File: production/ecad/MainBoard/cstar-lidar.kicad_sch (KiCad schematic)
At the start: 0 parts

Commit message: Added Lidar Connector
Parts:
- added J1: 532610771, 532610771:MOLEX_532610771, symbol 532610771:532610771
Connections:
- new net GND: J1.3, J1.4
- new net P3V3: J1.2
- new net P5V: J1.1, J1.5
- new net RX: J1.7
- new net TX: J1.6
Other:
- note added: "Lidar Connector"
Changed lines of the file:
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@@
 (kicad_sch (version 20230121) (generator eeschema)
   (paper "A4")
+  (wire (pts (xy 134.62 60.96) (xy 124.46 60.96))
+    (stroke (width 0) (type default))
+  )
+  (wire (pts (xy 124.46 66.04) (xy 134.62 66.04))
+    (stroke (width 0) (type default))
+  )
+  (wire (pts (xy 124.46 63.5) (xy 134.62 63.5))
+    (stroke (width 0) (type default))
+  )
+  (wire (pts (xy 124.46 73.66) (xy 134.62 73.66))
+    (stroke (width 0) (type default))
+  )
+  (wire (pts (xy 124.46 68.58) (xy 134.62 68.58))
+    (stroke (width 0) (type default))
+  )
+  (wire (pts (xy 124.46 71.12) (xy 134.62 71.12))
+    (stroke (width 0) (type default))
+  )
+  (wire (pts (xy 124.46 76.2) (xy 134.62 76.2))
+    (stroke (width 0) (type default))
+  )
+  (text "Lidar Connector\n" (at 134.62 53.34 0)
+    (effects (font (size 2 2)) (justify left bottom))
+  )
+  (label "GND" (at 124.46 68.58 0) (fields_autoplaced)
+    (effects (font (size 1.27 1.27)) (justify left bottom))
+  )
+  (label "TX" (at 124.46 73.66 0) (fields_autoplaced)
+    (effects (font (size 1.27 1.27)) (justify left bottom))
+  )
+  (label "GND" (at 124.46 66.04 0) (fields_autoplaced)
+    (effects (font (size 1.27 1.27)) (justify left bottom))
+  )
+  (label "RX" (at 124.46 76.2 0) (fields_autoplaced)
+    (effects (font (size 1.27 1.27)) (justify left bottom))
+  )
+  (label "P5V" (at 124.46 60.96 0) (fields_autoplaced)
+    (effects (font (size 1.27 1.27)) (justify left bottom))
+  )
+  (label "P5V" (at 124.46 71.12 0) (fields_autoplaced)
+    (effects (font (size 1.27 1.27)) (justify left bottom))
+  )
+  (label "P3V3" (at 124.46 63.5 0) (fields_autoplaced)
+    (effects (font (size 1.27 1.27)) (justify left bottom))
+  )
+  (symbol (lib_id "532610771:532610771") (at 147.32 71.12 0) (unit 1)
+    (in_bom yes) (on_board yes) (dnp no) (fields_autoplaced)
+    (property "Reference" "J1" (at 156.21 71.12 0)
+      (effects (font (size 1.27 1.27)) (justify left))
+    )
+    (property "Value" "532610771" (at 156.21 73.66 0)
+      (effects (font (size 1.27 1.27)) (justify left))
+    )
+    (property "Footprint" "532610771:MOLEX_532610771" (at 147.32 71.12 0)
+      (effects (font (size 1.27 1.27)) (justify bottom) hide)
+    )
+    (property "Datasheet" "" (at 147.32 71.12 0)
+      (effects (font (size 1.27 1.27)) hide)
+    )
+    (property "DigiKey_Part_Number" "WM7625TR-ND" (at 147.32 71.12 0)
+      (effects (font (size 1.27 1.27)) (justify bottom) hide)
+    )
+    (property "MF" "Molex" (at 147.32 71.12 0)
+      (effects (font (size 1.27 1.27)) (justify bottom) hide)
+    )
+    (property "MAXIMUM_PACKAGE_HEIGHT" "3.4 mm" (at 147.32 71.12 0)
+      (effects (font (size 1.27 1.27)) (justify bottom) hide)
+    )
+    (property "Package" "None" (at 147.32 71.12 0)
+      (effects (font (size 1.27 1.27)) (justify bottom) hide)
+    )
+    (property "Check_prices" "https://www.snapeda.com/parts/0532610771/Molex/view-part/?ref=eda" (at 147.32 71.12 0)
+      (effects (font (size 1.27 1.27)) (justify bottom) hide)
+    )
+    (property "STANDARD" "Manufacturer Recommendations" (at 147.32 71.12 0)
+      (effects (font (size 1.27 1.27)) (justify bottom) hide)
+    )
+    (property "PARTREV" "J" (at 147.32 71.12 0)
+      (effects (font (size 1.27 1.27)) (justify bottom) hide)
+    )
+    (property "SnapEDA_Link" "https://www.snapeda.com/parts/0532610771/Molex/view-part/?ref=snap" (at 147.32 71.12 0)
+      (effects (font (size 1.27 1.27)) (justify bottom) hide)
+    )
+    (property "MP" "0532610771" (at 147.32 71.12 0)
+      (effects (font (size 1.27 1.27)) (justify bottom) hide)
+    )
+    (property "Purchase-URL" "https://www.snapeda.com/api/url_track_click_mouser/?unipart_id=577144&manufacturer=Molex&part_name=0532610771&search_term=None" (at 147.32 71.12 0)
+      (effects (font (size 1.27 1.27)) (justify bottom) hide)
+    )
+    (property "Description" "\nPicoblade Connector, 7 Circuit Single Row, Right Angle Surface Mount SMT PCB\n" (at 147.32 71.12 0)
+      (effects (font (size 1.27 1.27)) (justify bottom) hide)
+    )
+    (property "MANUFACTURER" "Molex" (at 147.32 71.12 0)
+      (effects (font (size 1.27 1.27)) (justify bottom) hide)
+    )
+    (pin "S2")
+    (pin "2")
+    (pin "3")
+    (pin "S1")
+    (pin "5")
+    (pin "4")
+    (pin "6")
+    (pin "7")
+    (pin "1")
+    (instances
+      (project "cstar-lidar"
+        (path "/f4254b98-3297-4812-862b-6470cd23e6be"
+          (reference "J1") (unit 1)
+        )
+      )
+    )
+  )
+  (sheet_instances
+    (path "/" (page "1"))
+  )
 )

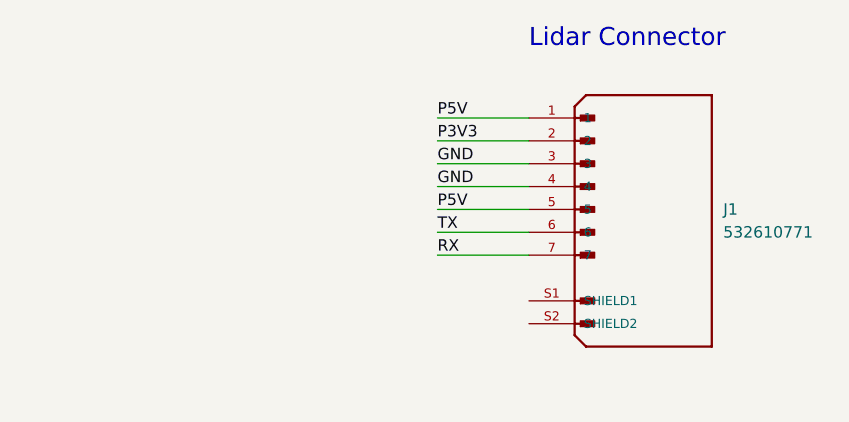
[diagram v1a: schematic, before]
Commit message: Added global and hierarchical connection for the lidar connector
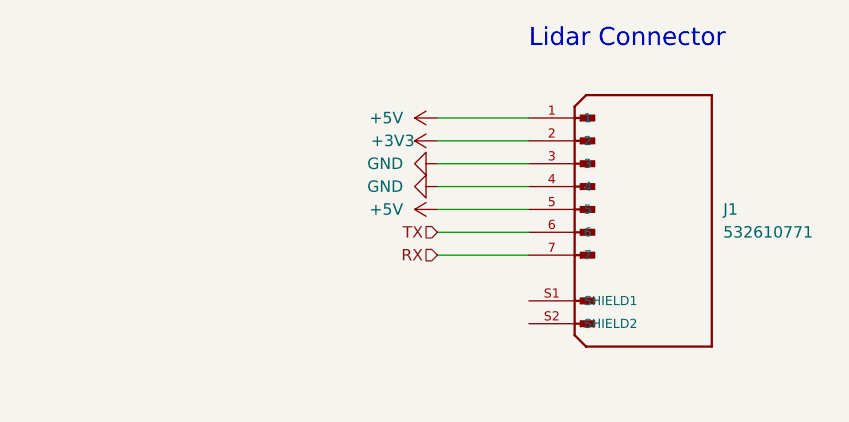
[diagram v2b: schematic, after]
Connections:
- net P3V3 renamed +3V3
- net P5V renamed +5V
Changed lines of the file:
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@@
     (effects (font (size 2 2)) (justify left bottom))
   )
-  (label "GND" (at 124.46 68.58 0) (fields_autoplaced)
-    (effects (font (size 1.27 1.27)) (justify left bottom))
+  (hierarchical_label "RX" (shape input) (at 124.46 76.2 180) (fields_autoplaced)
+    (effects (font (size 1.27 1.27)) (justify right))
   )
-  (label "TX" (at 124.46 73.66 0) (fields_autoplaced)
-    (effects (font (size 1.27 1.27)) (justify left bottom))
+  (hierarchical_label "TX" (shape input) (at 124.46 73.66 180) (fields_autoplaced)
+    (effects (font (size 1.27 1.27)) (justify right))
   )
-  (label "GND" (at 124.46 66.04 0) (fields_autoplaced)
-    (effects (font (size 1.27 1.27)) (justify left bottom))
+  (symbol (lib_id "power:GND") (at 124.46 68.58 270) (unit 1)
+    (in_bom yes) (on_board yes) (dnp no) (fields_autoplaced)
+    (property "Reference" "#PWR04" (at 118.11 68.58 0)
+      (effects (font (size 1.27 1.27)) hide)
+    )
+    (property "Value" "GND" (at 120.65 68.58 90)
+      (effects (font (size 1.27 1.27)) (justify right))
+    )
+    (property "Footprint" "" (at 124.46 68.58 0)
+      (effects (font (size 1.27 1.27)) hide)
+    )
+    (property "Datasheet" "" (at 124.46 68.58 0)
+      (effects (font (size 1.27 1.27)) hide)
+    )
+    (pin "1")
+    (instances
+      (project "cstar-lidar"
+        (path "/f4254b98-3297-4812-862b-6470cd23e6be"
+          (reference "#PWR04") (unit 1)
+        )
+      )
+    )
   )
-  (label "RX" (at 124.46 76.2 0) (fields_autoplaced)
-    (effects (font (size 1.27 1.27)) (justify left bottom))
+  (symbol (lib_id "power:GND") (at 124.46 66.04 270) (unit 1)
+    (in_bom yes) (on_board yes) (dnp no) (fields_autoplaced)
+    (property "Reference" "#PWR02" (at 118.11 66.04 0)
+      (effects (font (size 1.27 1.27)) hide)
+    )
+    (property "Value" "GND" (at 120.65 66.04 90)
+      (effects (font (size 1.27 1.27)) (justify right))
+    )
+    (property "Footprint" "" (at 124.46 66.04 0)
+      (effects (font (size 1.27 1.27)) hide)
+    )
+    (property "Datasheet" "" (at 124.46 66.04 0)
+      (effects (font (size 1.27 1.27)) hide)
+    )
+    (pin "1")
+    (instances
+      (project "cstar-lidar"
+        (path "/f4254b98-3297-4812-862b-6470cd23e6be"
+          (reference "#PWR02") (unit 1)
+        )
+      )
+    )
   )
-  (label "P5V" (at 124.46 60.96 0) (fields_autoplaced)
-    (effects (font (size 1.27 1.27)) (justify left bottom))
-  )
-  (label "P5V" (at 124.46 71.12 0) (fields_autoplaced)
-    (effects (font (size 1.27 1.27)) (justify left bottom))
-  )
-  (label "P3V3" (at 124.46 63.5 0) (fields_autoplaced)
-    (effects (font (size 1.27 1.27)) (justify left bottom))
+  (symbol (lib_id "power:+5V") (at 124.46 60.96 90) (unit 1)
+    (in_bom yes) (on_board yes) (dnp no) (fields_autoplaced)
+    (property "Reference" "#PWR03" (at 128.27 60.96 0)
+      (effects (font (size 1.27 1.27)) hide)
+    )
+    (property "Value" "+5V" (at 120.65 60.96 90)
+      (effects (font (size 1.27 1.27)) (justify left))
+    )
+    (property "Footprint" "" (at 124.46 60.96 0)
+      (effects (font (size 1.27 1.27)) hide)
+    )
+    (property "Datasheet" "" (at 124.46 60.96 0)
+      (effects (font (size 1.27 1.27)) hide)
+    )
+    (pin "1")
+    (instances
+      (project "cstar-lidar"
+        (path "/f4254b98-3297-4812-862b-6470cd23e6be"
+          (reference "#PWR03") (unit 1)
+        )
+      )
+    )
   )
   (symbol (lib_id "532610771:532610771") (at 147.32 71.12 0) (unit 1)
@@
         )
       )
+    )
+  )
+  (symbol (lib_id "power:+3V3") (at 124.46 63.5 90) (unit 1)
+    (in_bom yes) (on_board yes) (dnp no)
+    (property "Reference" "#PWR01" (at 128.27 63.5 0)
+      (effects (font (size 1.27 1.27)) hide)
+    )
+    (property "Value" "+3V3" (at 121.92 63.5 90)
+      (effects (font (size 1.27 1.27)) (justify left))
+    )
+    (property "Footprint" "" (at 124.46 63.5 0)
+      (effects (font (size 1.27 1.27)) hide)
+    )
+    (property "Datasheet" "" (at 124.46 63.5 0)
+      (effects (font (size 1.27 1.27)) hide)
+    )
+    (pin "1")
+    (instances
+      (project "cstar-lidar"
+        (path "/f4254b98-3297-4812-862b-6470cd23e6be"
+          (reference "#PWR01") (unit 1)
+        )
+      )
+    )
+  )
+  (symbol (lib_id "power:+5V") (at 124.46 71.12 90) (unit 1)
+    (in_bom yes) (on_board yes) (dnp no) (fields_autoplaced)
+    (property "Reference" "#PWR05" (at 128.27 71.12 0)
+      (effects (font (size 1.27 1.27)) hide)
+    )
+    (property "Value" "+5V" (at 120.65 71.12 90)
+      (effects (font (size 1.27 1.27)) (justify left))
+    )
+    (property "Footprint" "" (at 124.46 71.12 0)
+      (effects (font (size 1.27 1.27)) hide)
+    )
+    (property "Datasheet" "" (at 124.46 71.12 0)
+      (effects (font (size 1.27 1.27)) hide)
+    )
+    (pin "1")
+    (instances
+      (project "cstar-lidar"
+        (path "/f4254b98-3297-4812-862b-6470cd23e6be"
+          (reference "#PWR05") (unit 1)
+        )
+      )

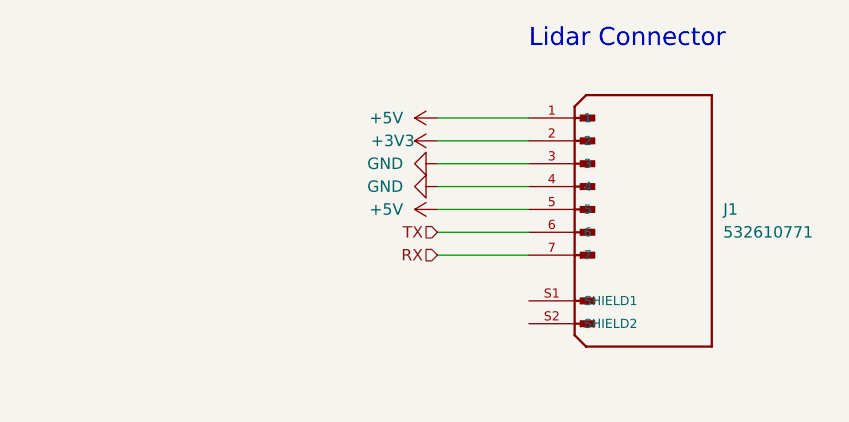
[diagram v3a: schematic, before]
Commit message: Added TVS Diode, NC flags, diode to i/o, LEDs to each power rail
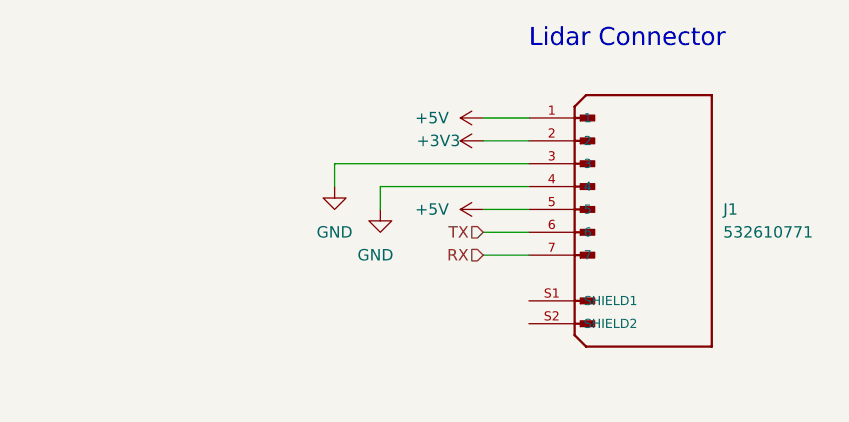
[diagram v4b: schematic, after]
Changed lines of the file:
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@@
 (kicad_sch (version 20230121) (generator eeschema)
   (paper "A4")
-  (wire (pts (xy 134.62 60.96) (xy 124.46 60.96))
-    (stroke (width 0) (type default))
-  )
-  (wire (pts (xy 124.46 66.04) (xy 134.62 66.04))
-    (stroke (width 0) (type default))
-  )
-  (wire (pts (xy 124.46 63.5) (xy 134.62 63.5))
-    (stroke (width 0) (type default))
-  )
-  (wire (pts (xy 124.46 73.66) (xy 134.62 73.66))
-    (stroke (width 0) (type default))
-  )
-  (wire (pts (xy 124.46 68.58) (xy 134.62 68.58))
-    (stroke (width 0) (type default))
-  )
-  (wire (pts (xy 124.46 71.12) (xy 134.62 71.12))
-    (stroke (width 0) (type default))
-  )
-  (wire (pts (xy 124.46 76.2) (xy 134.62 76.2))
+  (wire (pts (xy 113.03 66.04) (xy 134.62 66.04))
+    (stroke (width 0) (type default))
+  )
+  (wire (pts (xy 134.62 60.96) (xy 129.54 60.96))
+    (stroke (width 0) (type default))
+  )
+  (wire (pts (xy 129.54 63.5) (xy 134.62 63.5))
+    (stroke (width 0) (type default))
+  )
+  (wire (pts (xy 129.54 73.66) (xy 134.62 73.66))
+    (stroke (width 0) (type default))
+  )
+  (wire (pts (xy 118.11 68.58) (xy 118.11 71.12))
+    (stroke (width 0) (type default))
+  )
+  (wire (pts (xy 118.11 68.58) (xy 134.62 68.58))
+    (stroke (width 0) (type default))
+  )
+  (wire (pts (xy 113.03 66.04) (xy 113.03 68.58))
+    (stroke (width 0) (type default))
+  )
+  (wire (pts (xy 129.54 71.12) (xy 134.62 71.12))
+    (stroke (width 0) (type default))
+  )
+  (wire (pts (xy 129.54 76.2) (xy 134.62 76.2))
     (stroke (width 0) (type default))
   )
@@
     (effects (font (size 2 2)) (justify left bottom))
   )
-  (hierarchical_label "RX" (shape input) (at 124.46 76.2 180) (fields_autoplaced)
+  (hierarchical_label "RX" (shape input) (at 129.54 76.2 180) (fields_autoplaced)
     (effects (font (size 1.27 1.27)) (justify right))
   )
-  (hierarchical_label "TX" (shape input) (at 124.46 73.66 180) (fields_autoplaced)
+  (hierarchical_label "TX" (shape input) (at 129.54 73.66 180) (fields_autoplaced)
     (effects (font (size 1.27 1.27)) (justify right))
   )
-  (symbol (lib_id "power:GND") (at 124.46 68.58 270) (unit 1)
-    (in_bom yes) (on_board yes) (dnp no) (fields_autoplaced)
-    (property "Reference" "#PWR04" (at 118.11 68.58 0)
-      (effects (font (size 1.27 1.27)) hide)
-    )
-    (property "Value" "GND" (at 120.65 68.58 90)
-      (effects (font (size 1.27 1.27)) (justify right))
-    )
-    (property "Footprint" "" (at 124.46 68.58 0)
-      (effects (font (size 1.27 1.27)) hide)
-    )
-    (property "Datasheet" "" (at 124.46 68.58 0)
+  (symbol (lib_id "power:GND") (at 118.11 71.12 0) (unit 1)
+    (in_bom yes) (on_board yes) (dnp no)
+    (property "Reference" "#PWR04" (at 118.11 77.47 0)
+      (effects (font (size 1.27 1.27)) hide)
+    )
+    (property "Value" "GND" (at 115.57 76.2 0)
+      (effects (font (size 1.27 1.27)) (justify left))
+    )
+    (property "Footprint" "" (at 118.11 71.12 0)
+      (effects (font (size 1.27 1.27)) hide)
+    )
+    (property "Datasheet" "" (at 118.11 71.12 0)
       (effects (font (size 1.27 1.27)) hide)
     )
@@
     )
   )
-  (symbol (lib_id "power:GND") (at 124.46 66.04 270) (unit 1)
-    (in_bom yes) (on_board yes) (dnp no) (fields_autoplaced)
-    (property "Reference" "#PWR02" (at 118.11 66.04 0)
-      (effects (font (size 1.27 1.27)) hide)
-    )
-    (property "Value" "GND" (at 120.65 66.04 90)
-      (effects (font (size 1.27 1.27)) (justify right))
-    )
-    (property "Footprint" "" (at 124.46 66.04 0)
-      (effects (font (size 1.27 1.27)) hide)
-    )
-    (property "Datasheet" "" (at 124.46 66.04 0)
-      (effects (font (size 1.27 1.27)) hide)
-    )
-    (pin "1")
-    (instances
-      (project "CSTAR"
-        (path "/cd9fa943-c6eb-468b-990c-ea873c442553/3e924a05-61af-4a8a-bc82-0b26814a19c7"
+  (symbol (lib_id "power:+5V") (at 129.54 60.96 90) (unit 1)
+    (in_bom yes) (on_board yes) (dnp no) (fields_autoplaced)
+    (property "Reference" "#PWR03" (at 133.35 60.96 0)
+      (effects (font (size 1.27 1.27)) hide)
+    )
+    (property "Value" "+5V" (at 125.73 60.96 90)
+      (effects (font (size 1.27 1.27)) (justify left))
+    )
+    (property "Footprint" "" (at 129.54 60.96 0)
+      (effects (font (size 1.27 1.27)) hide)
+    )
+    (property "Datasheet" "" (at 129.54 60.96 0)
+      (effects (font (size 1.27 1.27)) hide)
+    )
+    (pin "1")
+    (instances
+      (project "CSTAR"
+        (path "/cd9fa943-c6eb-468b-990c-ea873c442553/3e924a05-61af-4a8a-bc82-0b26814a19c7"
+          (reference "#PWR03") (unit 1)
+        )
+      )
+      (project "cstar-lidar"
+        (path "/f4254b98-3297-4812-862b-6470cd23e6be"
+          (reference "#PWR03") (unit 1)
+        )
+      )
+    )
+  )
+  (symbol (lib_id "power:GND") (at 113.03 68.58 0) (unit 1)
+    (in_bom yes) (on_board yes) (dnp no) (fields_autoplaced)
+    (property "Reference" "#PWR02" (at 113.03 74.93 0)
+      (effects (font (size 1.27 1.27)) hide)
+    )
+    (property "Value" "GND" (at 113.03 73.66 0)
+      (effects (font (size 1.27 1.27)))
+    )
+    (property "Footprint" "" (at 113.03 68.58 0)
+      (effects (font (size 1.27 1.27)) hide)
+    )
+    (property "Datasheet" "" (at 113.03 68.58 0)
+      (effects (font (size 1.27 1.27)) hide)
+    )
+    (pin "1")
+    (instances
+      (project "cstar-lidar"
+        (path "/f4254b98-3297-4812-862b-6470cd23e6be"
           (reference "#PWR02") (unit 1)
-        )
-      )
-      (project "cstar-lidar"
-        (path "/f4254b98-3297-4812-862b-6470cd23e6be"
-          (reference "#PWR02") (unit 1)
-        )
-      )
-    )
-  )
-  (symbol (lib_id "power:+5V") (at 124.46 60.96 90) (unit 1)
-    (in_bom yes) (on_board yes) (dnp no) (fields_autoplaced)
-    (property "Reference" "#PWR03" (at 128.27 60.96 0)
-      (effects (font (size 1.27 1.27)) hide)
-    )
-    (property "Value" "+5V" (at 120.65 60.96 90)
-      (effects (font (size 1.27 1.27)) (justify left))
-    )
-    (property "Footprint" "" (at 124.46 60.96 0)
-      (effects (font (size 1.27 1.27)) hide)
-    )
-    (property "Datasheet" "" (at 124.46 60.96 0)
-      (effects (font (size 1.27 1.27)) hide)
-    )
-    (pin "1")
-    (instances
-      (project "CSTAR"
-        (path "/cd9fa943-c6eb-468b-990c-ea873c442553/3e924a05-61af-4a8a-bc82-0b26814a19c7"
-          (reference "#PWR03") (unit 1)
-        )
-      )
-      (project "cstar-lidar"
-        (path "/f4254b98-3297-4812-862b-6470cd23e6be"
-          (reference "#PWR03") (unit 1)
         )
       )
@@
     )
   )
-  (symbol (lib_id "power:+3V3") (at 124.46 63.5 90) (unit 1)
+  (symbol (lib_id "power:+3V3") (at 129.54 63.5 90) (unit 1)
     (in_bom yes) (on_board yes) (dnp no)
-    (property "Reference" "#PWR01" (at 128.27 63.5 0)
-      (effects (font (size 1.27 1.27)) hide)
-    )
-    (property "Value" "+3V3" (at 121.92 63.5 90)
-      (effects (font (size 1.27 1.27)) (justify left))
-    )
-    (property "Footprint" "" (at 124.46 63.5 0)
-      (effects (font (size 1.27 1.27)) hide)
-    )
-    (property "Datasheet" "" (at 124.46 63.5 0)
+    (property "Reference" "#PWR01" (at 133.35 63.5 0)
+      (effects (font (size 1.27 1.27)) hide)
+    )
+    (property "Value" "+3V3" (at 127 63.5 90)
+      (effects (font (size 1.27 1.27)) (justify left))
+    )
+    (property "Footprint" "" (at 129.54 63.5 0)
+      (effects (font (size 1.27 1.27)) hide)
+    )
+    (property "Datasheet" "" (at 129.54 63.5 0)
       (effects (font (size 1.27 1.27)) hide)
     )
@@
     )
   )
-  (symbol (lib_id "power:+5V") (at 124.46 71.12 90) (unit 1)
-    (in_bom yes) (on_board yes) (dnp no) (fields_autoplaced)
-    (property "Reference" "#PWR05" (at 128.27 71.12 0)
-      (effects (font (size 1.27 1.27)) hide)
-    )
-    (property "Value" "+5V" (at 120.65 71.12 90)
-      (effects (font (size 1.27 1.27)) (justify left))
-    )
-    (property "Footprint" "" (at 124.46 71.12 0)
-      (effects (font (size 1.27 1.27)) hide)
-    )
-    (property "Datasheet" "" (at 124.46 71.12 0)
-      (effects (font (size 1.27 1.27)) hide)
-    )
+  (symbol (lib_id "power:+5V") (at 129.54 71.12 90) (unit 1)
+    (in_bom yes) (on_board yes) (dnp no) (fields_autoplaced)
+    (property "Reference" "#PWR05" (at 133.35 71.12 0)
+      (effects (font (size 1.27 1.27)) hide)
+    )
+    (property "Value" "+5V" (at 125.73 71.12 90)
+      (effects (font (size 1.27 1.27)) (justify left))
+    )
+    (property "Footprint" "" (at 129.54 71.12 0)
+      (effects (font (size 1.27 1.27)) hide)
+    )
+    (property "Datasheet" "" (at 129.54 71.12 0)
+      (effects (font (size 1.27 1.27)) hide)
+    )
